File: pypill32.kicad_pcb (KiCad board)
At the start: 2 copper layers, 52.1 x 27.9 mm, 45 parts, among them J1 HeaderR, J2 HeaderL, J4 ISP, SW1 RST_BTN, SW2 BOOT_BTN, U1 SRV05-4, U2 PY32F030F18P6, U3 CH340N, U4 AMS1117-3.3, Y1 32.768 kHz

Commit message: checking and verifying still
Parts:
- removed REF**: ESD-Logo_6.6x6mm_SilkScreen, Symbol:ESD-Logo_6.6x6mm_SilkScreen
- added J3: USB_PINS, Connector_PinHeader_2.00mm:PinHeader_1x04_P2.00mm_Vertical, F.Cu at (93.8, 72.7)
- C13, C8: value 12p TSEKKAA -> 12p
- J4: value ISP -> SWD_HEADER
- moved C10 6.12 mm to (111.9, 70.8), turned to 0 degrees
- moved R5 1.70 mm to (118.6, 72.7)
- moved R6 1.45 mm to (118.6, 74.9)
- moved R3 0.63 mm to (101.3, 73.5)
- moved U1 0.59 mm to (105.6, 73.3), turned to 180 degrees
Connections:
- J2 pad 10: /PA3 -> PYURX
- J2 pad 9: /PA2 -> PYUTX
- R5 pad 2: /PF1 -> PYURX
- R6 pad 2: /PF0 -> PYUTX
- U2 pad 5: /PA2 -> PYUTX
- U2 pad 6: /PA3 -> PYURX
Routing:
- net PYURX: track 0.00 -> 19.6 mm
- net PYUTX: track 0.00 -> 18.6 mm
- net VBUS: track 25.8 -> 35.9 mm
- net /PA2: track 9.77 -> 0.00 mm
- net /PA3: track 8.98 -> 0.00 mm
- net GND: track 100.7 -> 108.3 mm, vias 134 -> 131
- net /PF1: track 21.4 -> 14.3 mm
- net USB_D+: track 18.9 -> 22.9 mm
- net /PF0: track 20.2 -> 16.6 mm
- net USB_D-: track 20.4 -> 22.5 mm
- net +3V3: track 88.1 -> 89.0 mm
- net +5V: track 33.6 -> 34.5 mm
- net Net-(U3-TXD): track 3.78 -> 3.14 mm
- net Net-(USB1-CC1): track 3.53 -> 4.16 mm
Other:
- board text added: "B"
- board text added: "D+"
- board text added: "D-"
- board text added: "PY32 F030"
- board text added: "R"
- board text added: "USB"
- board text added: "Vb"
- board text added: "rev.A"
- board text removed: "ESD"

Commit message: some fine-tuning
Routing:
- net GND: track 108.3 -> 108.4 mm, vias 131 -> 132
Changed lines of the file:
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@@
 			(plot_on_all_layers_selection 0x0000000_00000000)
 			(disableapertmacros no)
-			(usegerberextensions no)
+			(usegerberextensions yes)
 			(usegerberattributes yes)
 			(usegerberadvancedattributes yes)
-			(creategerberjobfile yes)
+			(creategerberjobfile no)
 			(dashed_line_dash_ratio 12.000000)
 			(dashed_line_gap_ratio 3.000000)
@@
 			(psa4output no)
 			(plotreference yes)
-			(plotvalue yes)
+			(plotvalue no)
 			(plotfptext yes)
 			(plotinvisibletext no)
 			(sketchpadsonfab no)
-			(subtractmaskfromsilk no)
+			(subtractmaskfromsilk yes)
 			(outputformat 1)
 			(mirror no)
-			(drillshape 1)
+			(drillshape 0)
 			(scaleselection 1)
-			(outputdirectory "")
+			(outputdirectory "gerbers/")
 		)
 	)
@@
 	)
 	(via
+		(at 102.362 69.5452)
+		(size 0.6)
+		(drill 0.3)
+		(layers "F.Cu" "B.Cu")
+		(free yes)
+		(net 3)
+	)
+	(via
 		(at 108.0008 63.1952)
 		(size 0.6)
@@
 	)
 	(segment
+		(start 112.522 71.0399)
+		(end 112.4409 71.0399)
+		(width 0.6)
+		(layer "B.Cu")
+		(net 3)
+	)
+	(segment
 		(start 109.22 87.63)
 		(end 109.22 88.0364)
@@
 	)
 	(segment
-		(start 114.4176 68.9516)
-		(end 116.1288 70.6628)
+		(start 109.3884 68.9516)
+		(end 114.9764 68.9516)
 		(width 1)
 		(layer "B.Cu")
@@
 	)
 	(segment
-		(start 104.14 67.0853)
-		(end 105.4823 68.4276)
+		(start 106.8324 68.4276)
+		(end 108.8644 68.4276)
 		(width 1)
 		(layer "B.Cu")
@@
 	)
 	(segment
-		(start 109.3884 68.9516)
-		(end 114.4176 68.9516)
+		(start 116.1288 78.3844)
+		(end 115.824 78.6892)
+		(width 1)
+		(layer "B.Cu")
+		(net 5)
+	)
+	(segment
+		(start 104.14 67.0853)
+		(end 105.4823 68.4276)
 		(width 1)
 		(layer "B.Cu")
@@
 	)
 	(segment
-		(start 116.1288 70.6628)
-		(end 116.1288 78.3844)
+		(start 115.824 78.6892)
+		(end 110.9472 78.6892)
 		(width 1)
 		(layer "B.Cu")
@@
 	)
 	(segment
-		(start 106.8324 68.4276)
-		(end 108.8644 68.4276)
+		(start 114.9764 68.9516)
+		(end 116.1288 70.104)
 		(width 1)
 		(layer "B.Cu")
@@
 	)
 	(segment
-		(start 116.1288 78.3844)
-		(end 115.824 78.6892)
-		(width 1)
-		(layer "B.Cu")
-		(net 5)
-	)
-	(segment
-		(start 115.824 78.6892)
-		(end 110.9472 78.6892)
+		(start 116.1288 70.104)
+		(end 116.1288 78.3844)
 		(width 1)
 		(layer "B.Cu")
@@
 	)
 	(segment
-		(start 133.5024 86.6648)
-		(end 133.5024 88.9)
-		(width 0.3)
-		(layer "F.Cu")
-		(net 13)
-	)
-	(segment
 		(start 112.8272 80.9752)
 		(end 106.5272 80.9752)
@@
 	)
 	(segment
+		(start 133.5024 88.9)
+		(end 133.5024 86.6648)
+		(width 0.6)
+		(layer "F.Cu")
+		(net 13)
+	)
+	(segment
 		(start 114.554 72.6948)
 		(end 113.1316 72.6948)
@@
 	)
 	(segment
+		(start 119.5832 82.6516)
+		(end 119.5832 82.3175)
+		(width 1)
+		(layer "B.Cu")
+		(net 13)
+	)
+	(segment
 		(start 133.5024 86.6648)
-		(end 133.7056 86.4616)
+		(end 133.604 86.5632)
 		(width 0.6)
 		(layer "B.Cu")
@@
 	)
 	(segment
-		(start 133.7056 86.4616)
-		(end 133.7056 80.645)
+		(start 133.604 86.5632)
+		(end 133.604 80.7466)
 		(width 0.6)
 		(layer "B.Cu")
@@
 	)
 	(segment
-		(start 119.5832 82.6516)
-		(end 119.5832 82.3175)
-		(width 1)
+		(start 133.604 80.7466)
+		(end 133.7056 80.645)
+		(width 0.6)
 		(layer "B.Cu")
 		(net 13)
@@
 	)
 	(segment
-		(start 125.8824 75.4888)
-		(end 125.8824 76.7588)
+		(start 136.4488 77.0128)
+		(end 137.5664 78.1304)
 		(width 0.3)
 		(layer "B.Cu")
@@
 	)
 	(segment
-		(start 136.398 76.962)
-		(end 137.5664 78.1304)
+		(start 137.5664 78.1304)
+		(end 139.3444 78.1304)
 		(width 0.3)
 		(layer "B.Cu")
@@
 	)
 	(segment
-		(start 137.5664 78.1304)
-		(end 139.3444 78.1304)
+		(start 125.8824 76.7588)
+		(end 126.1364 77.0128)
 		(width 0.3)
 		(layer "B.Cu")
@@
 	)
 	(segment
-		(start 125.8824 76.7588)
-		(end 126.0856 76.962)
+		(start 126.1364 77.0128)
+		(end 136.4488 77.0128)
 		(width 0.3)
 		(layer "B.Cu")
@@
 	)
 	(segment
-		(start 126.0856 76.962)
-		(end 136.398 76.962)
+		(start 125.8824 75.4888)
+		(end 125.8824 76.7588)
 		(width 0.3)
 		(layer "B.Cu")
@@
 	)
 	(segment
-		(start 127.3302 75.2602)
-		(end 138.938 75.2602)
+		(start 132.1816 75.0824)
+		(end 132.5372 75.438)
+		(width 0.3)
+		(layer "B.Cu")
+		(net 30)
+	)
+	(segment
+		(start 127.508 75.0824)
+		(end 132.1816 75.0824)
 		(width 0.3)
 		(layer "B.Cu")
@@
 	)
 	(segment
-		(start 138.938 75.2602)
+		(start 138.811 75.438)
 		(end 138.938 75.565)
 		(width 0.3)
@@
 	)
 	(segment
+		(start 132.5372 75.438)
+		(end 138.811 75.438)
+		(width 0.3)
+		(layer "B.Cu")
+		(net 30)
+	)
+	(segment
+		(start 127.3302 75.2602)
+		(end 127.508 75.0824)
+		(width 0.3)
+		(layer "B.Cu")
+		(net 30)
+	)
+	(segment
 		(start 114.6048 86.0552)
 		(end 113.0808 86.0552)
@@
 	)
 	(segment
-		(start 134.6962 77.9526)
-		(end 133.6454 77.9526)
-		(width 0.3)
+		(start 133.6454 77.9526)
+		(end 133.35 78.248)
+		(width 0.6)
 		(layer "F.Cu")
 		(net 36)
 	)
 	(segment
-		(start 122.7744 73.4152)
-		(end 123.0388 73.6796)
-		(width 0.3)
+		(start 134.6962 77.9526)
+		(end 133.6454 77.9526)
+		(width 0.6)
 		(layer "F.Cu")
 		(net 36)
 	)
 	(segment
-		(start 133.6454 77.9526)
-		(end 133.35 78.248)
+		(start 122.7744 73.4152)
+		(end 123.0388 73.6796)
 		(width 0.3)
 		(layer "F.Cu")
@@
 	)
 	(segment
+		(start 131.4216 68.9356)
+		(end 133.1976 70.7116)
+		(width 0.6)
+		(layer "F.Cu")
+		(net 37)
+	)
+	(segment
 		(start 122.0216 84.836)
 		(end 119.7864 84.836)
@@
 	)
 	(segment
-		(start 131.4876 69.5116)
-		(end 133.1976 69.5116)
-		(width 0.3)
-		(layer "F.Cu")
-		(net 37)
-	)
-	(segment
 		(start 124.3388 78.2008)
 		(end 124.3388 79.4046)
@@
 	(segment
 		(start 130.9116 68.9356)
-		(end 131.4876 69.5116)
-		(width 0.3)
+		(end 131.4216 68.9356)
+		(width 0.6)
 		(layer "F.Cu")
 		(net 37)
@@
 		(start 133.5024 82.3)
 		(end 133.5024 80.4004)
-		(width 0.3)
+		(width 0.6)
 		(layer "F.Cu")
 		(net 38)
 	)
 	(segment
-		(start 133.5024 80.4004)
+		(start 133.2992 80.2988)
 		(end 133.35 80.248)
 		(width 0.3)
@@
 	)
 	(segment
-		(start 133.2992 80.2988)
+		(start 133.5024 80.4004)
 		(end 133.35 80.248)
-		(width 0.3)
+		(width 0.6)
 		(layer "F.Cu")
 		(net 38)

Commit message: LICENSE
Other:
- board text added: "CERN-OHL-W"
- board text removed: "Open HW: CERN OHL"
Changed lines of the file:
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@@
 		)
 	)
-	(gr_text "Open HW:\nCERN OHL"
-		(at 105.5116 80.772 0)
+	(gr_text "CERN-OHL-W"
+		(at 101.8032 79.6544 0)
 		(layer "B.SilkS")
 		(effects
@@
 				(bold yes)
 			)
-			(justify left bottom mirror)
+			(justify bottom mirror)
 		)
 	)

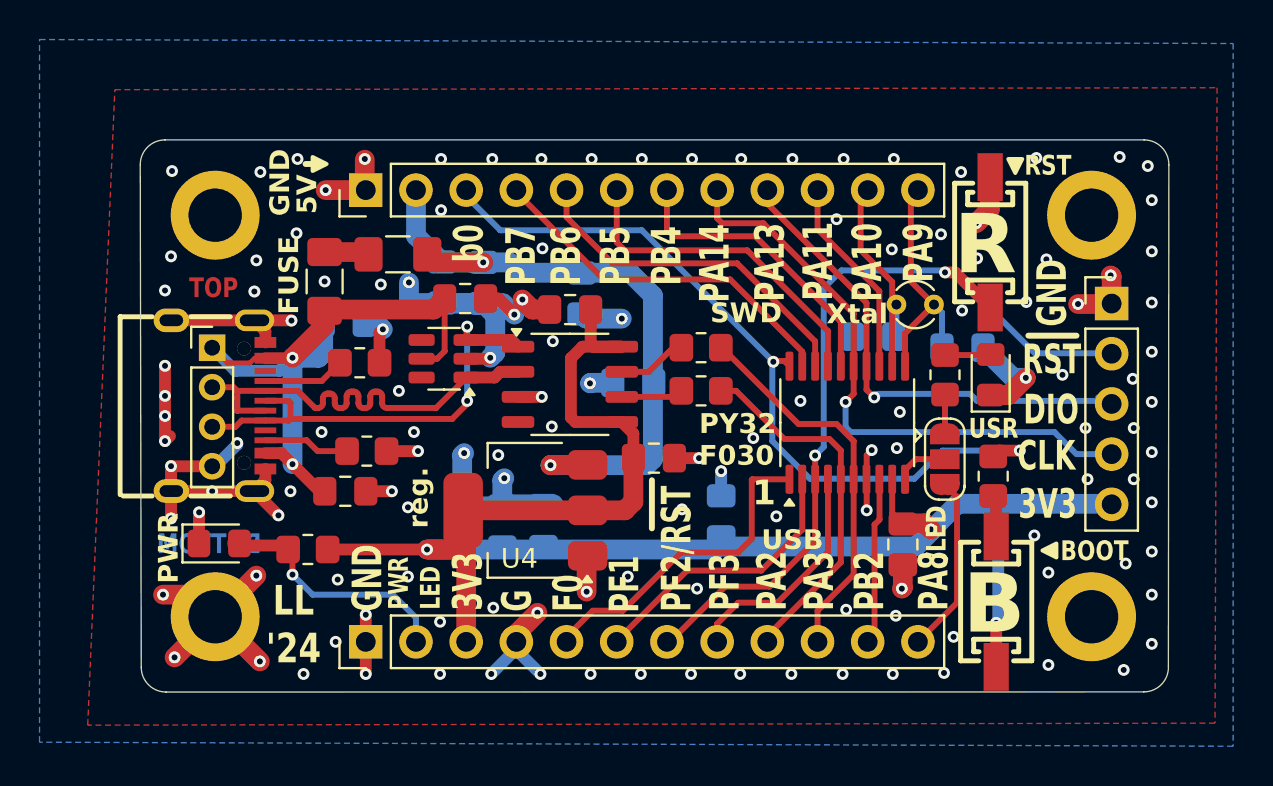
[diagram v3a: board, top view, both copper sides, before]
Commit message: fix uart pins
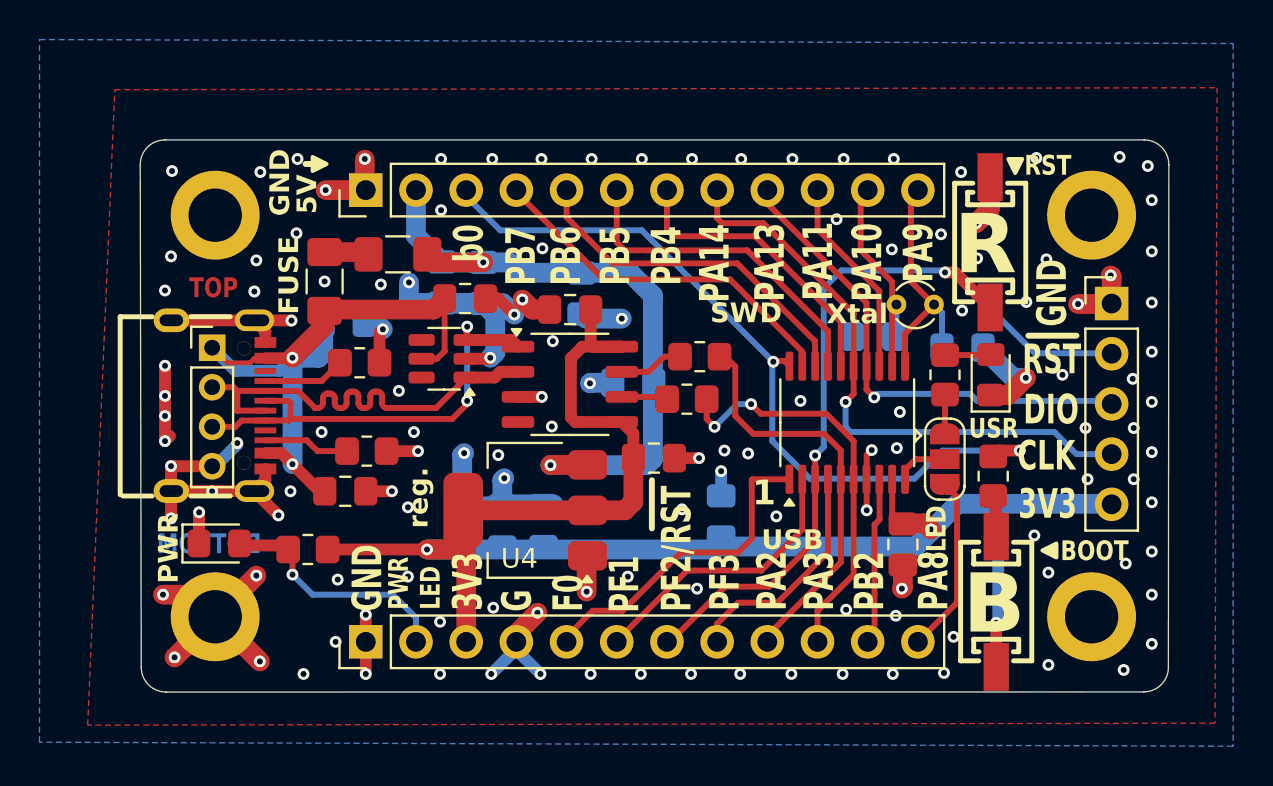
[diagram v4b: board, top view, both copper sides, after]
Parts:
- moved R6 0.83 mm to (117.8, 75.3)
- moved R5 0.46 mm to (118.5, 73.2)
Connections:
- R5 pad 2: PYURX -> PYUTX
- R6 pad 2: PYUTX -> PYURX
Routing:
- net PYUTX: track 18.6 -> 21.3 mm
- net PYURX: track 19.6 -> 20.8 mm, vias 0 -> 2
- net Net-(U3-TXD): track 3.14 -> 2.34 mm
- net GND: vias 132 -> 133
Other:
- board text removed: "PY32 F030"
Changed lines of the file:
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@@
 		(tags "capacitor handsolder")
 		(property "Reference" "C10"
-			(at 0.1016 1.6256 360)
+			(at 0.1016 1.6256 0)
 			(layer "F.SilkS")
 			(hide yes)
@@
 		)
 		(property "Value" "100nF"
-			(at 0 1.68 360)
+			(at 0 1.68 0)
 			(layer "F.Fab")
 			(effects
@@
 		)
 		(property "Footprint" "Capacitor_SMD:C_0805_2012Metric_Pad1.18x1.45mm_HandSolder"
-			(at 0 0 360)
+			(at 0 0 0)
 			(layer "F.Fab")
 			(hide yes)
@@
 		)
 		(property "Datasheet" ""
-			(at 0 0 360)
+			(at 0 0 0)
 			(layer "F.Fab")
 			(hide yes)
@@
 		)
 		(property "Description" ""
-			(at 0 0 360)
+			(at 0 0 0)
 			(layer "F.Fab")
 			(hide yes)
@@
 		)
 		(fp_text user "${REFERENCE}"
-			(at 0 0 360)
+			(at 0 0 0)
 			(layer "F.Fab")
 			(effects
@@
 	(footprint "Resistor_SMD:R_0805_2012Metric_Pad1.20x1.40mm_HandSolder"
 		(layer "F.Cu")
-		(at 118.5672 72.7456)
+		(at 118.5 73.2)
 		(descr "Resistor SMD 0805 (2012 Metric), square (rectangular) end terminal, IPC_7351 nominal with elongated pad for handsoldering. (Body size source: IPC-SM-782 page 72, https://www.pcb-3d.com/wordpress/wp-content/uploads/ipc-sm-782a_amendment_1_and_2.pdf), generated with kicad-footprint-generator")
 		(tags "resistor handsolder")
@@
 			(layers "F.Cu" "F.Paste" "F.Mask")
 			(roundrect_rratio 0.208333)
-			(net 34 "PYURX")
+			(net 35 "PYUTX")
 			(pintype "passive")
 		)
@@
 	(footprint "Resistor_SMD:R_0805_2012Metric_Pad1.20x1.40mm_HandSolder"
 		(layer "F.Cu")
-		(at 118.5672 74.93)
+		(at 117.85 75.35)
 		(descr "Resistor SMD 0805 (2012 Metric), square (rectangular) end terminal, IPC_7351 nominal with elongated pad for handsoldering. (Body size source: IPC-SM-782 page 72, https://www.pcb-3d.com/wordpress/wp-content/uploads/ipc-sm-782a_amendment_1_and_2.pdf), generated with kicad-footprint-generator")
 		(tags "resistor handsolder")
 		(property "Reference" "R6"
-			(at 2.5654 -0.0762 0)
+			(at 2.5654 -0.0762 360)
 			(layer "F.SilkS")
 			(hide yes)
@@
 		)
 		(property "Value" "0R"
-			(at 0 1.65 0)
+			(at 0 1.65 360)
 			(layer "F.Fab")
 			(effects
@@
 		)
 		(property "Footprint" "Resistor_SMD:R_0805_2012Metric_Pad1.20x1.40mm_HandSolder"
-			(at 0 0 0)
+			(at 0 0 360)
 			(layer "F.Fab")
 			(hide yes)
@@
 		)
 		(property "Datasheet" ""
-			(at 0 0 0)
+			(at 0 0 360)
 			(layer "F.Fab")
 			(hide yes)
@@
 		)
 		(property "Description" ""
-			(at 0 0 0)
+			(at 0 0 360)
 			(layer "F.Fab")
 			(hide yes)
@@
 		)
 		(fp_text user "${REFERENCE}"
-			(at 0 0 0)
+			(at 0 0 360)
 			(layer "F.Fab")
 			(effects
@@
 			(layers "F.Cu" "F.Paste" "F.Mask")
 			(roundrect_rratio 0.208333)
-			(net 35 "PYUTX")
+			(net 34 "PYURX")
 			(pintype "passive")
 		)
@@
 		)
 		(property "Value" "SRV05-4"
-			(at 0 2.4 360)
+			(at 0 2.4 0)
 			(layer "F.Fab")
 			(effects
@@
 		)
 		(property "Footprint" "Package_TO_SOT_SMD:SOT-23-6"
-			(at 0 0 360)
+			(at 0 0 0)
 			(layer "F.Fab")
 			(hide yes)
@@
 		)
 		(property "Datasheet" "http://www.onsemi.com/pub/Collateral/SRV05-4-D.PDF"
-			(at 0 0 360)
+			(at 0 0 0)
 			(layer "F.Fab")
 			(hide yes)
@@
 		)
 		(property "Description" ""
-			(at 0 0 360)
+			(at 0 0 0)
 			(layer "F.Fab")
 			(hide yes)
@@
 		)
 		(fp_text user "${REFERENCE}"
-			(at 0 0 360)
+			(at 0 0 0)
 			(layer "F.Fab")
 			(effects
@@
 		)
 	)
-	(gr_text "LL\n'24"
-		(at 97.9424 88.8492 0)
-		(layer "F.SilkS")
-		(effects
-			(font
-				(size 1.5 1.2)
-				(thickness 0.3)
-				(bold yes)
-			)
-			(justify bottom)
-		)
-	)
 	(gr_text "PWR"
 		(at 92.202 84.6836 90)
@@
 		)
 	)
-	(gr_text "PY32\nF030"
-		(at 118.4656 78.7908 0)
-		(layer "F.SilkS")
-		(effects
-			(font
-				(size 1 1)
-				(thickness 0.25)
-				(bold yes)
-			)
-			(justify left bottom)
-		)
-	)
 	(gr_text "PB2"
 		(at 127.9652 86.0552 90)
@@
 	)
 	(segment
-		(start 114.554 73.9648)
-		(end 115.9256 73.9648)
+		(start 116.6904 73.2)
+		(end 117.5 73.2)
 		(width 0.3)
 		(layer "F.Cu")
@@
 	)
 	(segment
-		(start 117.1448 72.7456)
-		(end 117.5672 72.7456)
+		(start 114.554 73.9648)
+		(end 115.9256 73.9648)
 		(width 0.3)
 		(layer "F.Cu")
@@
 	(segment
 		(start 115.9256 73.9648)
-		(end 117.1448 72.7456)
+		(end 116.6904 73.2)
 		(width 0.3)
 		(layer "F.Cu")
@@
 	)
 	(via
-		(at 121.2088 77.3176)
+		(at 120.95 78.1)
 		(size 0.6)
 		(drill 0.3)
@@
 	)
 	(via
+		(at 119.75 77.95)
+		(size 0.6)
+		(drill 0.3)
+		(layers "F.Cu" "B.Cu")
+		(free yes)
+		(net 3)
+	)
+	(via
 		(at 98.1456 63.1952)
 		(size 0.6)
@@
 	)
 	(segment
-		(start 117.2624 75.2348)
-		(end 117.5672 74.93)
+		(start 116.7348 75.2348)
+		(end 116.85 75.35)
 		(width 0.3)
 		(layer "F.Cu")
@@
 	(segment
 		(start 114.554 75.2348)
-		(end 117.2624 75.2348)
+		(end 116.7348 75.2348)
 		(width 0.3)
 		(layer "F.Cu")
@@
 	)
 	(segment
-		(start 119.5672 72.7456)
-		(end 119.634 72.7456)
+		(start 124.46 86.0552)
+		(end 124.46 87.63)
 		(width 0.3)
 		(layer "F.Cu")
@@
 	)
 	(segment
-		(start 123.4948 76.6064)
-		(end 125.4252 76.6064)
+		(start 121.588 76.088)
+		(end 124.9068 76.088)
 		(width 0.3)
 		(layer "F.Cu")
@@
 	)
 	(segment
-		(start 124.46 86.0552)
-		(end 124.46 87.63)
+		(start 121.1 75.6)
+		(end 121.588 76.088)
 		(width 0.3)
 		(layer "F.Cu")
@@
 	)
 	(segment
-		(start 119.634 72.7456)
-		(end 123.4948 76.6064)
+		(start 118.85 76.35)
+		(end 119.25 76.75)
 		(width 0.3)
 		(layer "F.Cu")
@@
 	)
 	(segment
-		(start 126.2888 79.4046)
-		(end 126.2888 84.2264)
+		(start 118.85 75.35)
+		(end 118.85 76.35)
 		(width 0.3)
 		(layer "F.Cu")
@@
 	)
 	(segment
-		(start 125.4252 76.6064)
-		(end 126.2888 77.47)
+		(start 119.25 76.75)
+		(end 119.3 76.8)
+		(width 0.3)
+		(layer "F.Cu")
+		(net 34)
+	)
+	(segment
+		(start 126.2888 79.4046)
+		(end 126.2888 84.2264)
 		(width 0.3)
 		(layer "F.Cu")
@@
 	)
 	(segment
-		(start 120.3452 74.93)
-		(end 119.5672 74.93)
+		(start 124.9068 76.088)
+		(end 126.2888 77.47)
 		(width 0.3)
 		(layer "F.Cu")
-		(net 35)
+		(net 34)
+	)
+	(via
+		(at 119.25 76.75)
+		(size 0.6)
+		(drill 0.3)
+		(layers "F.Cu" "B.Cu")
+		(net 34)
+	)
+	(via
+		(at 121.1 75.6)
+		(size 0.6)
+		(drill 0.3)
+		(layers "F.Cu" "B.Cu")
+		(net 34)
+	)
+	(segment
+		(start 120.4 75.6)
+		(end 119.25 76.75)
+		(width 0.3)
+		(layer "B.Cu")
+		(net 34)
+	)
+	(segment
+		(start 121.1 75.6)
+		(end 120.4 75.6)
+		(width 0.3)
+		(layer "B.Cu")
+		(net 34)
 	)
 	(segment
@@
 	)
 	(segment
+		(start 125.6388 77.9376)
+		(end 124.8076 77.1064)
+		(width 0.3)
+		(layer "F.Cu")
+		(net 35)
+	)
+	(segment
 		(start 125.6388 83.6064)
 		(end 121.92 87.3252)
@@
 	)
 	(segment
+		(start 124.8076 77.1064)
+		(end 121.2064 77.1064)
+		(width 0.3)
+		(layer "F.Cu")
+		(net 35)
+	)
+	(segment
 		(start 125.6388 79.4046)
 		(end 125.6388 83.6064)
@@
 	)
 	(segment
-		(start 122.7836 77.3684)
-		(end 120.3452 74.93)
+		(start 119.634 73.066)
+		(end 119.634 72.7456)
 		(width 0.3)
 		(layer "F.Cu")
@@
 	)
 	(segment
-		(start 125.0696 77.3684)
-		(end 122.7836 77.3684)
+		(start 120.3 73.7)
+		(end 119.8 73.2)
 		(width 0.3)
 		(layer "F.Cu")
@@
 	)
 	(segment
-		(start 125.6388 77.9376)
-		(end 125.0696 77.3684)
+		(start 119.8 73.2)
+		(end 119.5 73.2)
+		(width 0.3)
+		(layer "F.Cu")
+		(net 35)
+	)
+	(segment
+		(start 121.2064 77.1064)
+		(end 120.3 76.2)
+		(width 0.3)
+		(layer "F.Cu")
+		(net 35)
+	)
+	(segment
+		(start 119.5 73.2)
+		(end 119.634 73.066)
+		(width 0.3)
+		(layer "F.Cu")
+		(net 35)
+	)
+	(segment
+		(start 120.3 76.2)
+		(end 120.3 73.7)
 		(width 0.3)
 		(layer "F.Cu")
